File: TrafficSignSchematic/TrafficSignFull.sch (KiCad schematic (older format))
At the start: 27 parts, among them J1 IDC connector, J2 3.96mm pitch 4-pin polarized 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, U1 ATmega328P-PU, U2 SIM800L, U3 BQ24650, Y1 16MHz

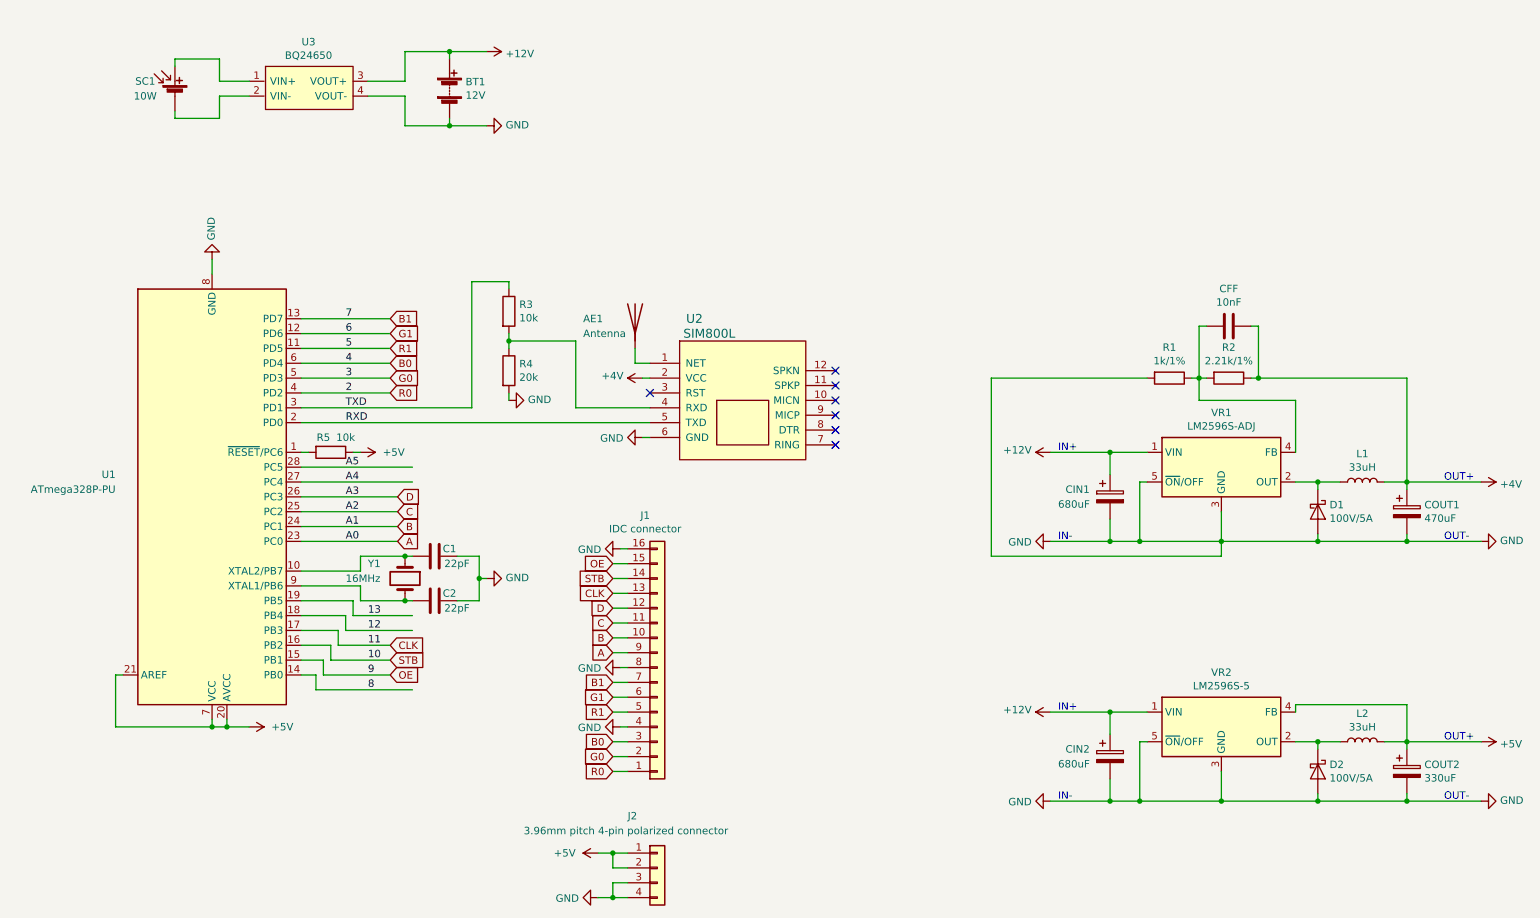
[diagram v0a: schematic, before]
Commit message: Added footprints to all elements
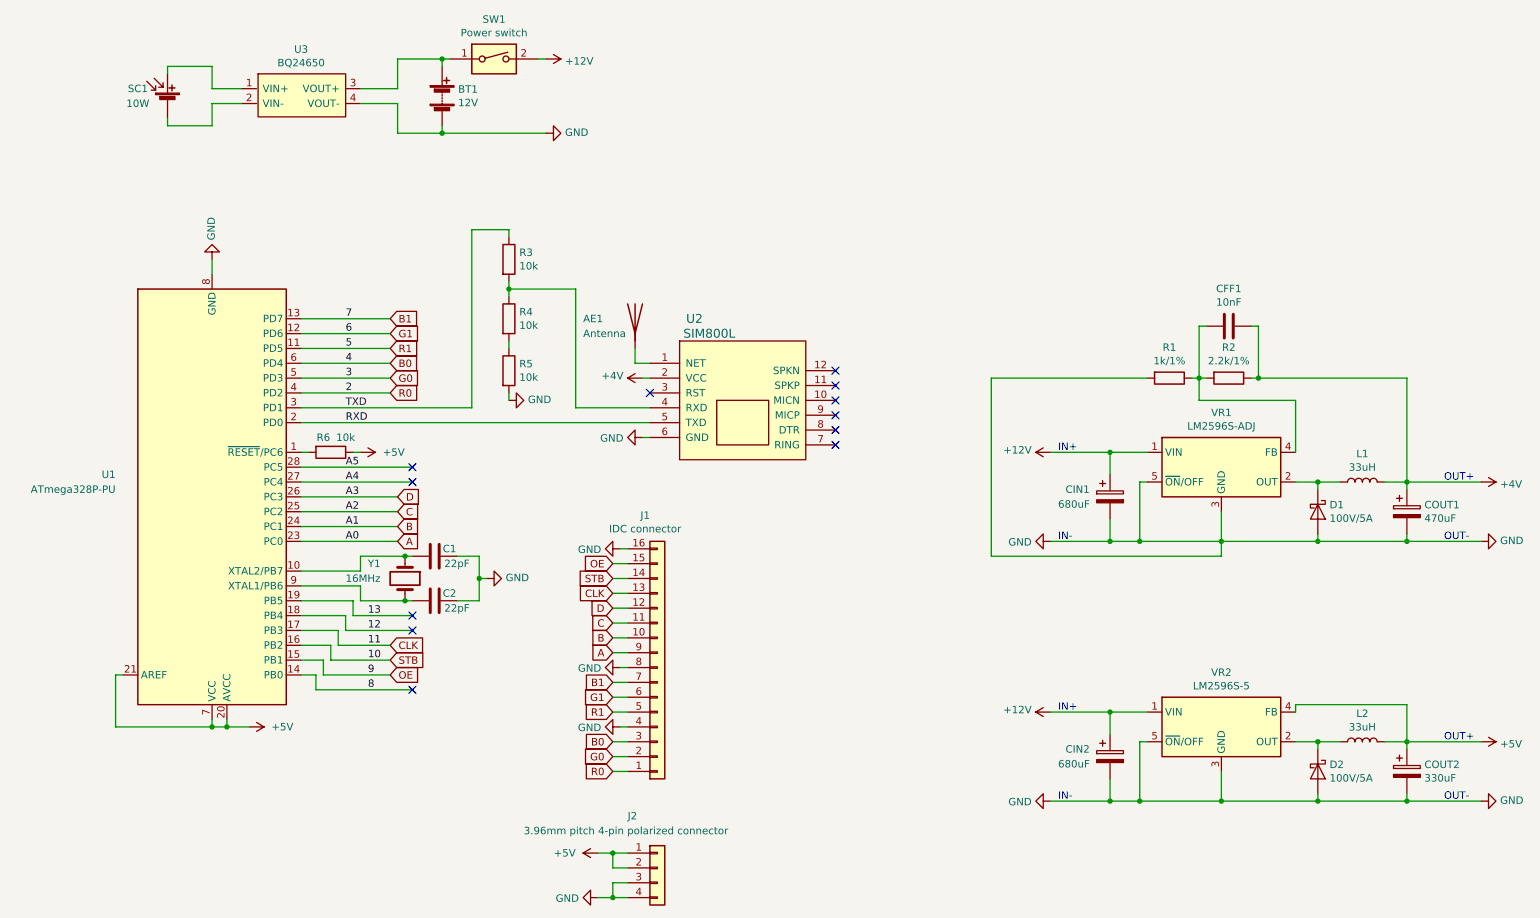
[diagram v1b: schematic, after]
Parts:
- added R5: 10k, Resistor_THT:R_Axial_DIN0204_L3.6mm_D1.6mm_P7.62mm_Horizontal, symbol Device:R
- added SW1: Power switch, symbol Switch:SW_DIP_x01
- CFF1: renamed from CFF; footprint (none) -> Capacitor_THT:C_Disc_D4.3mm_W1.9mm_P5.00mm
- CIN1, CIN2, COUT1, COUT2: footprint (none) -> Capacitor_THT:CP_Radial_D10.0mm_P5.00mm
- D1, D2: footprint (none) -> Diode_THT:D_DO-27_P15.24mm_Horizontal
- L1, L2: footprint (none) -> Inductor_SMD:L_Bourns_SDR1806
- R1: footprint (none) -> Resistor_THT:R_Axial_DIN0207_L6.3mm_D2.5mm_P10.16mm_Horizontal
- R2: value 2.21k/1% -> 2.2k/1%; footprint (none) -> Resistor_THT:R_Axial_DIN0207_L6.3mm_D2.5mm_P10.16mm_Horizontal
- R3: footprint (none) -> Resistor_THT:R_Axial_DIN0204_L3.6mm_D1.6mm_P7.62mm_Horizontal
- R4: value 20k -> 10k; footprint (none) -> Resistor_THT:R_Axial_DIN0204_L3.6mm_D1.6mm_P7.62mm_Horizontal
- R6: renamed from R5; footprint (none) -> Resistor_THT:R_Axial_DIN0204_L3.6mm_D1.6mm_P7.62mm_Horizontal
- Y1: footprint (none) -> Crystal:Crystal_HC49-U_Vertical
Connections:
- wire segments 171 -> 173
- no-connect marks 7 -> 12
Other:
- moved on the sheet: BT1, R3, SC1, U3
